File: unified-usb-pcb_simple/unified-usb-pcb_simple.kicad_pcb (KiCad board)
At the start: 2 copper layers, 30 x 35 mm, 11 parts, among them J1 USB_C_Receptacle_USB2.0, J2 USB_Out, U1 SRV05-4

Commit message: fixed name on silkscreen
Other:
- board text added: "Type-C PCB [simple] rev 1.0 github.com/ebastler/unified-usb-pcb mpwr.xyz"
- board text removed: "Type-C PCB [Li-Ion] rev 1.0 github.com/ebastler/unified-usb-pcb mpwr.xyz"
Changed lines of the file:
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@@
     (effects (font (size 1 1) (thickness 0.15)))
   )
-  (gr_text "Type-C PCB [Li-Ion] rev 1.0\ngithub.com/ebastler/unified-usb-pcb\nmpwr.xyz" (at 45.3644 45.085) (layer B.SilkS)
+  (gr_text "Type-C PCB [simple] rev 1.0\ngithub.com/ebastler/unified-usb-pcb\nmpwr.xyz" (at 45.3644 45.085) (layer B.SilkS)
     (effects (font (size 1 1) (thickness 0.15)) (justify left mirror))
   )
@@
   (segment (start 33.2094 28.228) (end 34.0614 29.08) (width 0.508) (layer F.Cu) (net 3))
   (segment (start 33.2094 27.588) (end 33.2094 28.228) (width 0.508) (layer F.Cu) (net 3))
-  (segment (start 30.3784 22.479) (end 24.4094 22.479) (width 0.254) (layer F.Cu) (net 8))
-  (segment (start 32.0094 25.9398) (end 32.0094 24.11) (width 0.254) (layer F.Cu) (net 8))
-  (segment (start 32.0094 24.11) (end 30.3784 22.479) (width 0.254) (layer F.Cu) (net 8))
-  (segment (start 22.6314 24.257) (end 22.6314 24.8665) (width 0.254) (layer F.Cu) (net 8))
-  (segment (start 24.4094 22.479) (end 22.6314 24.257) (width 0.254) (layer F.Cu) (net 8))
   (segment (start 31.8594 31.717001) (end 31.8594 30.922) (width 0.1905) (layer F.Cu) (net 4))
   (segment (start 30.95625 32.620151) (end 31.8594 31.717001) (width 0.1905) (layer F.Cu) (net 4))
@@
   (segment (start 30.0094 28.672) (end 30.0094 25.983) (width 0.1905) (layer F.Cu) (net 5))
   (segment (start 29.6594 29.022) (end 30.0094 28.672) (width 0.1905) (layer F.Cu) (net 5))
+  (segment (start 30.3784 22.479) (end 24.4094 22.479) (width 0.254) (layer F.Cu) (net 8))
+  (segment (start 32.0094 25.9398) (end 32.0094 24.11) (width 0.254) (layer F.Cu) (net 8))
+  (segment (start 32.0094 24.11) (end 30.3784 22.479) (width 0.254) (layer F.Cu) (net 8))
+  (segment (start 22.6314 24.257) (end 22.6314 24.8665) (width 0.254) (layer F.Cu) (net 8))
+  (segment (start 24.4094 22.479) (end 22.6314 24.257) (width 0.254) (layer F.Cu) (net 8))
   (segment (start 29.0094 25.9398) (end 29.0094 24.138) (width 0.254) (layer F.Cu) (net 10))
   (segment (start 28.2394 23.368) (end 25.1714 23.368) (width 0.254) (layer F.Cu) (net 10))

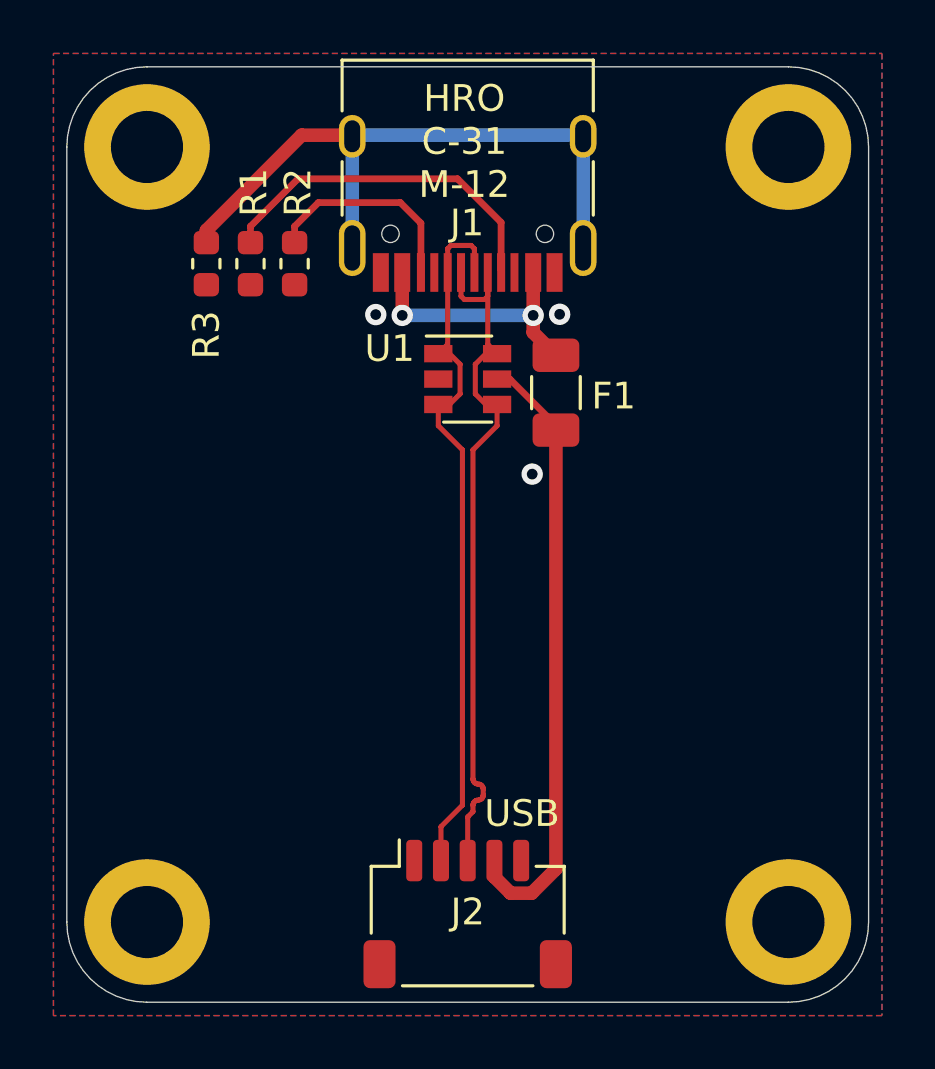
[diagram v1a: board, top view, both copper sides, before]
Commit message: added ferrite bead, improved usb track matching
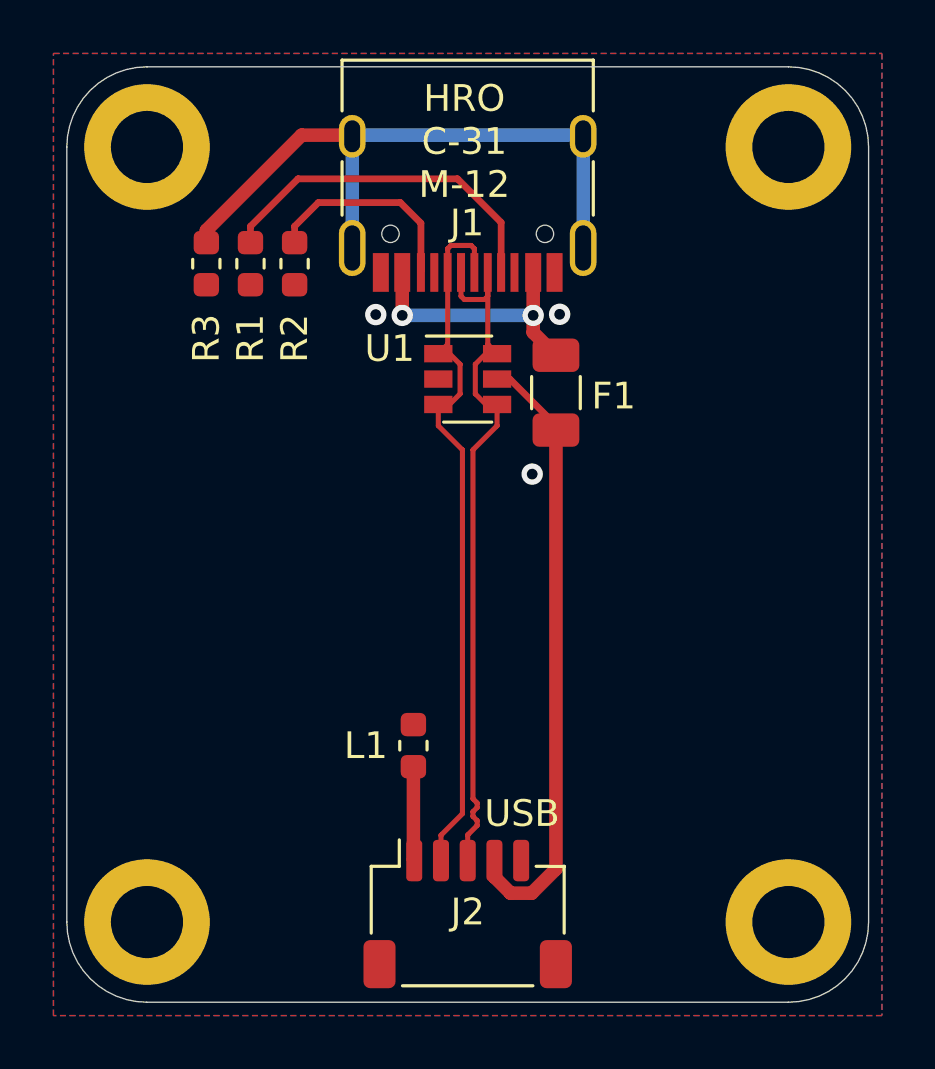
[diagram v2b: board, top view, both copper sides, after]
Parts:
- added L1: BLM18PG121SN1D, Inductor_SMD:L_0603_1608Metric, F.Cu at (28.7, 43.7)
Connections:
- J2 pad 1: GNDPWR -> GND
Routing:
- net GND: track 0.00 -> 3.53 mm

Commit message: moved outline/holes for usb-c connector to protrude 1 mm
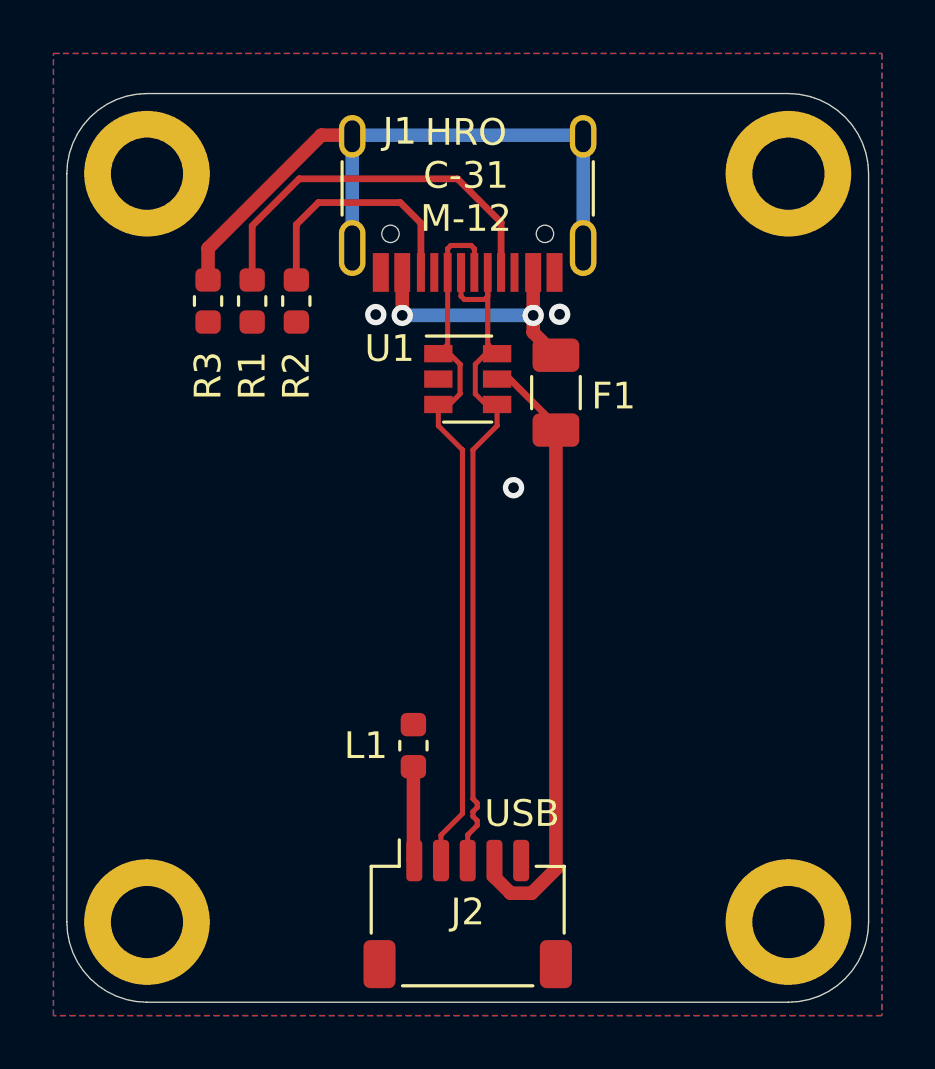
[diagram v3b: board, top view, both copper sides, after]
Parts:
- moved R1 1.40 mm to (22.7, 27.1)
- moved R2 1.40 mm to (24.3, 27.1)
- moved R3 1.40 mm to (21.0, 27.1)
- moved H1 1.00 mm to (18.8, 22.3)
- moved H2 1.00 mm to (42.8, 22.3)
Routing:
- net Net-(J1-PadB5): track 7.83 -> 9.20 mm
- net Net-(J1-PadA5): track 13.2 -> 14.6 mm
- net Net-(J1-PadS1): track 24.4 -> 25.3 mm
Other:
- board size 30 x 35 mm -> 30 x 34 mm

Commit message: created plane for usb-shielding below the connector
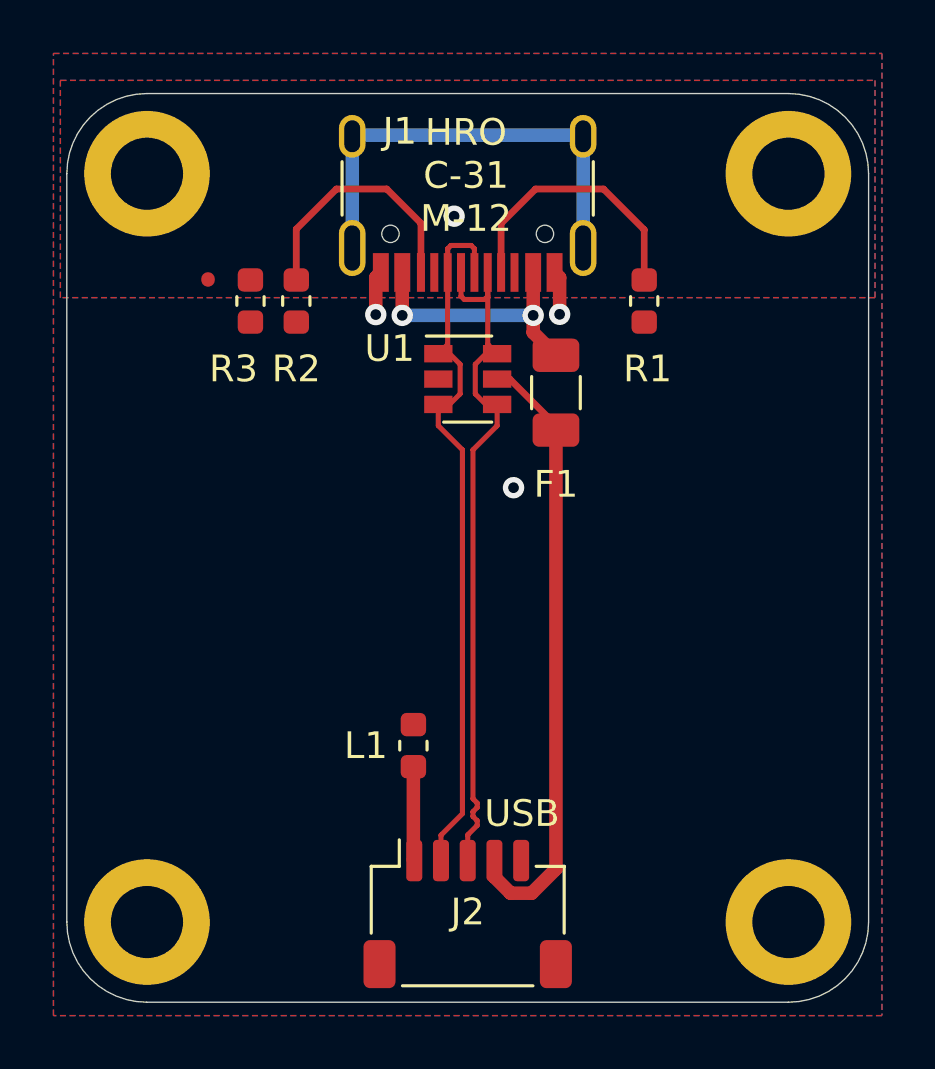
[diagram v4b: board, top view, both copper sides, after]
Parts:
- moved R1 14.7 mm to (37.4, 27.1)
- moved R3 1.59 mm to (22.6, 27.1)
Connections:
- H1 pad 1: GNDPWR -> Earth
- H2 pad 1: GNDPWR -> Earth
- J1 pad S1: Net-(J1-PadS1) -> Earth
- R3 pad 2: Net-(J1-PadS1) -> Earth
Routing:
- net Net-(J1-PadS1): track 25.3 -> 0.00 mm
- net Earth: track 0.00 -> 17.1 mm, vias 0 -> 1
- net Net-(J1-PadA5): track 14.6 -> 10.1 mm
- net GNDPWR: track 0.57 -> 3.87 mm
- added copper zone on B.Cu, net Earth
- added copper zone on F.Cu, net Earth

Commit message: resized shield plane
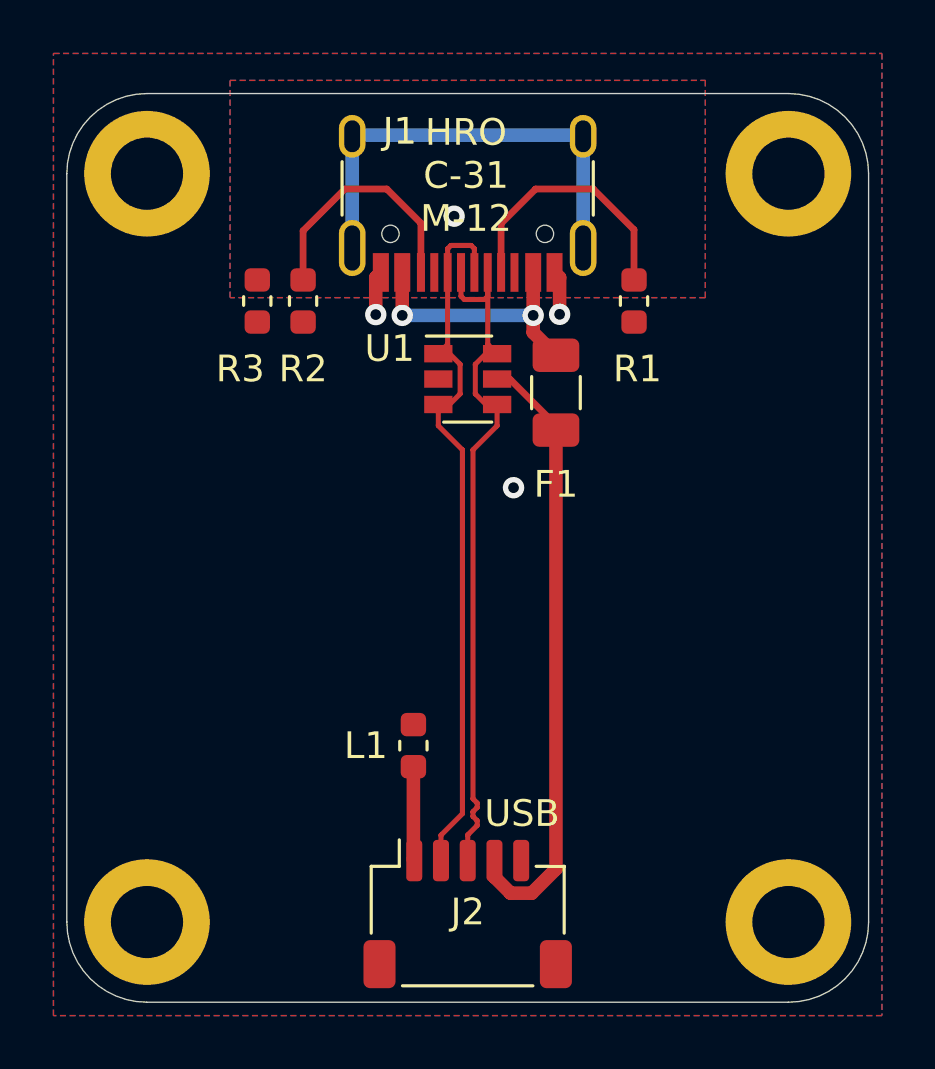
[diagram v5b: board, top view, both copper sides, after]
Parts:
- moved R1 0.38 mm to (37.0, 27.1)
- moved R2 0.25 mm to (24.6, 27.1)
- moved R3 0.25 mm to (22.9, 27.1)
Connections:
- H1 pad 1: Earth -> GNDPWR
- H2 pad 1: Earth -> GNDPWR
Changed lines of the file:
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@@
     (thickness 1.6)
     (drawings 11)
-    (tracks 83)
+    (tracks 82)
     (zones 0)
     (modules 12)
@@
     )
     (pad 1 thru_hole circle (at 0 0) (size 4.7 4.7) (drill 2.7) (layers *.Cu *.Mask)
-      (net 12 Earth))
+      (net 1 GNDPWR))
   )
   (module MountingHole:MountingHole_2.7mm_M2.5_DIN965_Pad (layer F.Cu)
@@
     )
     (pad 1 thru_hole circle (at 0 0) (size 4.7 4.7) (drill 2.7) (layers *.Cu *.Mask)
-      (net 12 Earth))
+      (net 1 GNDPWR))
   )
   (module Connector_JST:JST_SH_SM05B-SRSS-TB_1x05-1MP_P1.00mm_Horizontal (layer F.Cu)
@@
   )
   (module Resistor_SMD:R_0603_1608Metric (layer F.Cu)
-    (at 37.3634 27.051 90)
+    (at 36.9824 27.051 90)
     (descr "Resistor SMD 0603 (1608 Metric), square (rectangular) end terminal, IPC_7351 nominal, (Body size source: http://www.tortai-tech.com/upload/download/2011102023233369053.pdf), generated with kicad-footprint-generator")
     (tags resistor)
@@
   )
   (module Resistor_SMD:R_0603_1608Metric (layer F.Cu)
-    (at 24.3459 27.051 90)
+    (at 24.5999 27.051 90)
     (descr "Resistor SMD 0603 (1608 Metric), square (rectangular) end terminal, IPC_7351 nominal, (Body size source: http://www.tortai-tech.com/upload/download/2011102023233369053.pdf), generated with kicad-footprint-generator")
     (tags resistor)
@@
   )
   (module Resistor_SMD:R_0603_1608Metric (layer F.Cu)
-    (at 22.6314 27.051 90)
+    (at 22.8854 27.051 90)
     (descr "Resistor SMD 0603 (1608 Metric), square (rectangular) end terminal, IPC_7351 nominal, (Body size source: http://www.tortai-tech.com/upload/download/2011102023233369053.pdf), generated with kicad-footprint-generator")
     (tags resistor)
@@
   (segment (start 29.7594 47.988) (end 29.7594 47.038) (width 0.1905) (layer F.Cu) (net 5))
   (segment (start 29.7594 47.038) (end 30.56255 46.23485) (width 0.1905) (layer F.Cu) (net 5))
-  (segment (start 35.8394 22.86) (end 37.3634 24.384) (width 0.254) (layer F.Cu) (net 8))
+  (segment (start 35.4584 22.86) (end 36.9824 24.384) (width 0.254) (layer F.Cu) (net 8))
+  (segment (start 33.2994 22.86) (end 35.4584 22.86) (width 0.254) (layer F.Cu) (net 8))
   (segment (start 32.0094 25.983) (end 32.0094 24.15) (width 0.254) (layer F.Cu) (net 8))
-  (segment (start 37.3634 24.384) (end 37.3634 26.1365) (width 0.254) (layer F.Cu) (net 8))
-  (segment (start 33.2994 22.86) (end 35.8394 22.86) (width 0.254) (layer F.Cu) (net 8))
   (segment (start 32.0094 24.15) (end 33.2994 22.86) (width 0.254) (layer F.Cu) (net 8))
-  (segment (start 24.3459 24.36037) (end 24.3459 26.2635) (width 0.254) (layer F.Cu) (net 10))
-  (segment (start 25.84627 22.86) (end 24.3459 24.36037) (width 0.254) (layer F.Cu) (net 10))
-  (segment (start 27.7314 22.86) (end 25.84627 22.86) (width 0.254) (layer F.Cu) (net 10))
-  (segment (start 29.0094 25.9398) (end 29.0094 24.138) (width 0.254) (layer F.Cu) (net 10))
-  (segment (start 29.0094 24.138) (end 27.7314 22.86) (width 0.254) (layer F.Cu) (net 10))
+  (segment (start 36.9824 24.384) (end 36.9824 26.2635) (width 0.254) (layer F.Cu) (net 8))
+  (segment (start 27.7314 22.86) (end 29.0094 24.138) (width 0.254) (layer F.Cu) (net 10))
+  (segment (start 26.16377 22.86) (end 27.7314 22.86) (width 0.254) (layer F.Cu) (net 10))
+  (segment (start 29.0094 24.138) (end 29.0094 25.9398) (width 0.254) (layer F.Cu) (net 10))
+  (segment (start 24.5999 26.2635) (end 24.5999 24.42387) (width 0.254) (layer F.Cu) (net 10))
+  (segment (start 24.5999 24.42387) (end 26.16377 22.86) (width 0.254) (layer F.Cu) (net 10))
   (segment (start 35.0794 20.8448) (end 35.0794 25.0248) (width 0.508) (layer B.Cu) (net 12))
   (segment (start 26.4394 20.8448) (end 35.0794 20.8448) (width 0.508) (layer B.Cu) (net 12))
@@
   (via (at 30.2514 23.876) (size 0.8) (drill 0.4) (layers F.Cu B.Cu) (net 12))
   (segment (start 26.4246 20.8448) (end 26.4394 20.8448) (width 0.508) (layer F.Cu) (net 12))
-  (segment (start 21.0439 26.2635) (end 21.0439 26.2255) (width 0.508) (layer F.Cu) (net 12))
   (segment (start 28.7274 47.956) (end 28.7594 47.988) (width 0.508) (layer F.Cu) (net 11))
   (segment (start 28.7274 44.4755) (end 28.7274 47.956) (width 0.508) (layer F.Cu) (net 11))
@@
     (polygon
       (pts
-        (xy 45.9994 26.924) (xy 15.5194 26.924) (xy 15.5194 18.796) (xy 45.9994 18.796)
+        (xy 39.6494 26.924) (xy 21.8694 26.924) (xy 21.8694 18.796) (xy 39.6494 18.796)
       )
     )
@@
     (polygon
       (pts
-        (xy 45.9994 26.924) (xy 15.5194 26.924) (xy 15.5194 18.796) (xy 45.9994 18.796)
+        (xy 39.6494 26.924) (xy 21.8694 26.924) (xy 21.8694 18.796) (xy 39.6494 18.796)
       )
     )

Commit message: added manufacturing files
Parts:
- F1: value 1206L050/15YR -> SCF075-1206R
- L1: value BLM18PG121SN1D -> PBY160808T-181Y-N
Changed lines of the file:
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@@
   )
   (setup
-    (last_trace_width 0.254)
+    (last_trace_width 0.1905)
     (user_trace_width 0.254)
     (user_trace_width 0.3048)
@@
       (outputformat 1)
       (mirror false)
-      (drillshape 1)
+      (drillshape 0)
       (scaleselection 1)
-      (outputdirectory ""))
+      (outputdirectory "./"))
   )
   (net 0 "")
@@
       (effects (font (size 1 1) (thickness 0.15)))
     )
-    (fp_text value BLM18PG121SN1D (at 0 1.43 90) (layer F.Fab)
+    (fp_text value PBY160808T-181Y-N (at 0 1.43 90) (layer F.Fab)
       (effects (font (size 1 1) (thickness 0.15)))
     )
@@
       (effects (font (size 1 1) (thickness 0.15)))
     )
-    (fp_text value 1206L050/15YR (at 0 1.82 90) (layer F.Fab)
+    (fp_text value SCF075-1206R (at 0 1.82 90) (layer F.Fab)
       (effects (font (size 1 1) (thickness 0.15)))
     )
@@
   (segment (start 24.5999 26.2635) (end 24.5999 24.42387) (width 0.254) (layer F.Cu) (net 10))
   (segment (start 24.5999 24.42387) (end 26.16377 22.86) (width 0.254) (layer F.Cu) (net 10))
+  (segment (start 28.7274 47.956) (end 28.7594 47.988) (width 0.508) (layer F.Cu) (net 11))
+  (segment (start 28.7274 44.4755) (end 28.7274 47.956) (width 0.508) (layer F.Cu) (net 11))
   (segment (start 35.0794 20.8448) (end 35.0794 25.0248) (width 0.508) (layer B.Cu) (net 12))
   (segment (start 26.4394 20.8448) (end 35.0794 20.8448) (width 0.508) (layer B.Cu) (net 12))
@@
   (via (at 30.2514 23.876) (size 0.8) (drill 0.4) (layers F.Cu B.Cu) (net 12))
   (segment (start 26.4246 20.8448) (end 26.4394 20.8448) (width 0.508) (layer F.Cu) (net 12))
-  (segment (start 28.7274 47.956) (end 28.7594 47.988) (width 0.508) (layer F.Cu) (net 11))
-  (segment (start 28.7274 44.4755) (end 28.7274 47.956) (width 0.508) (layer F.Cu) (net 11))
   (zone (net 1) (net_name GNDPWR) (layer F.Cu) (hatch edge 0.508)
     (connect_pads (clearance 0.2032))
